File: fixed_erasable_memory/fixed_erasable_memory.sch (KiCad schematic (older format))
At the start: 1 part, among them P1 DIN_41612_128P

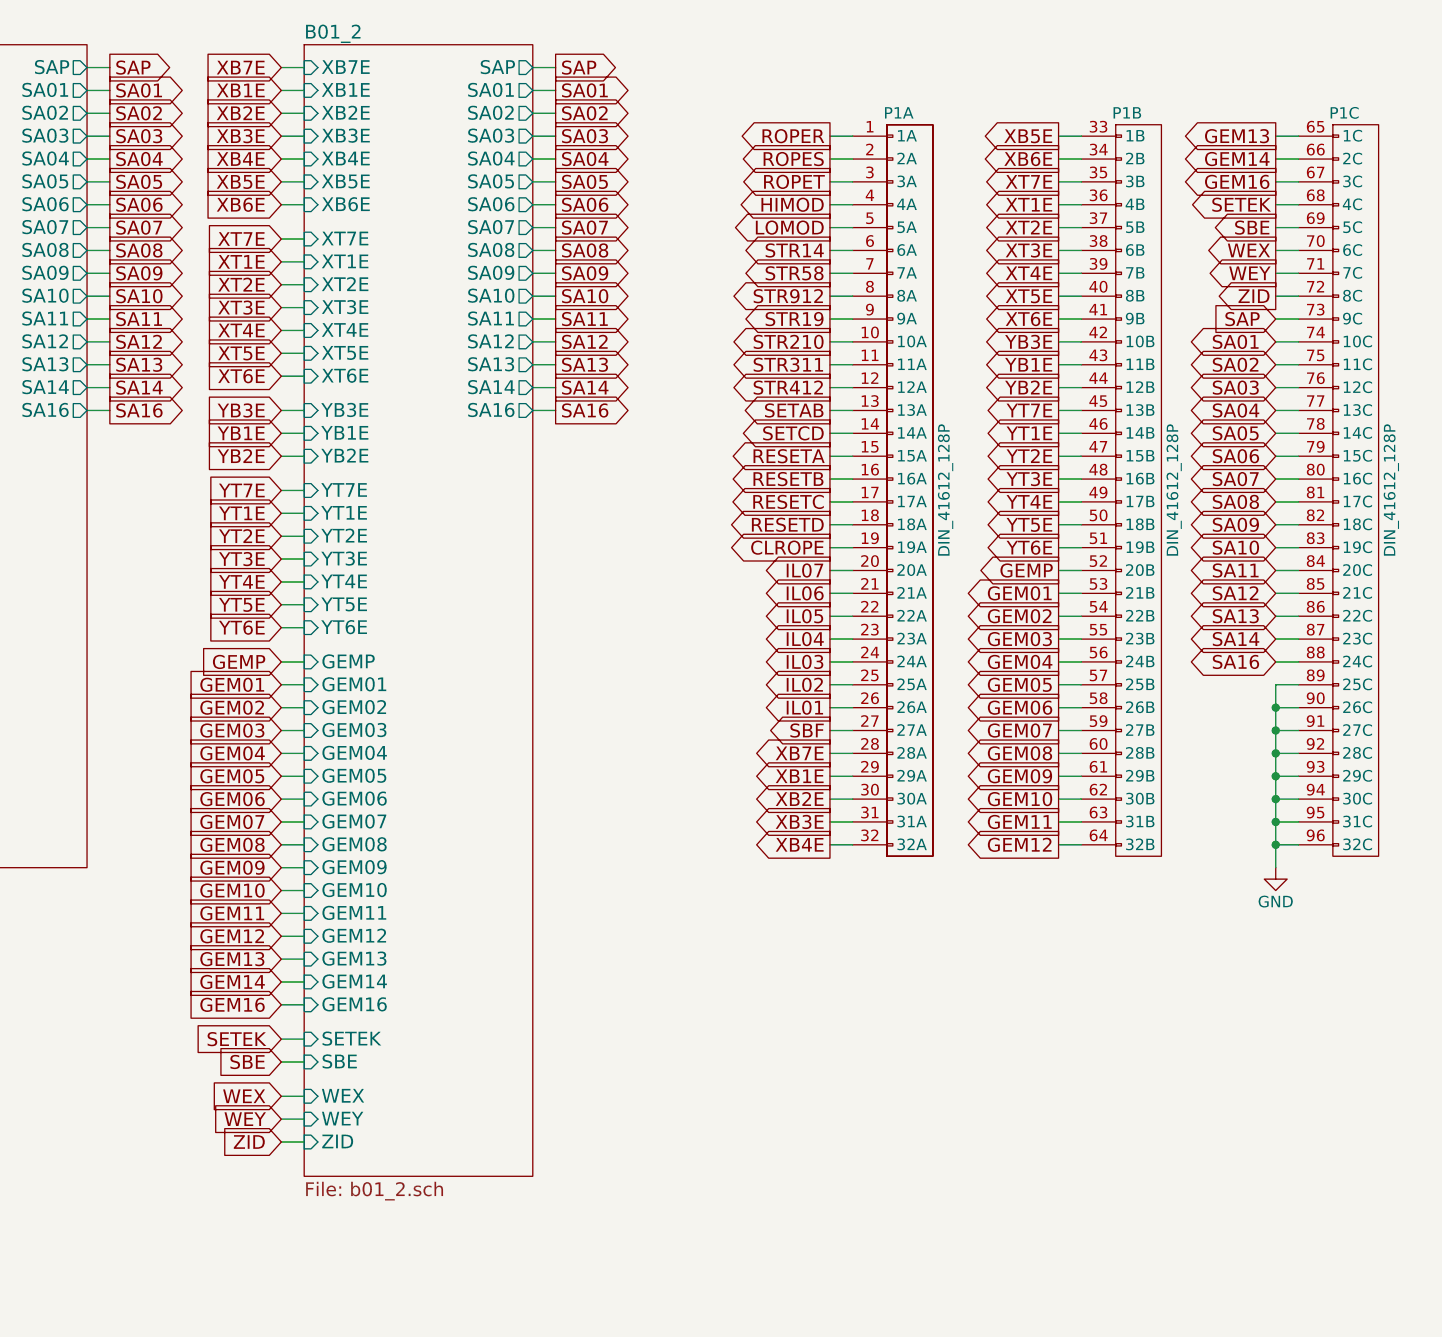
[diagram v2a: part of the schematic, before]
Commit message: Made erasable memory reads destructive, and improved erasable address latching logic
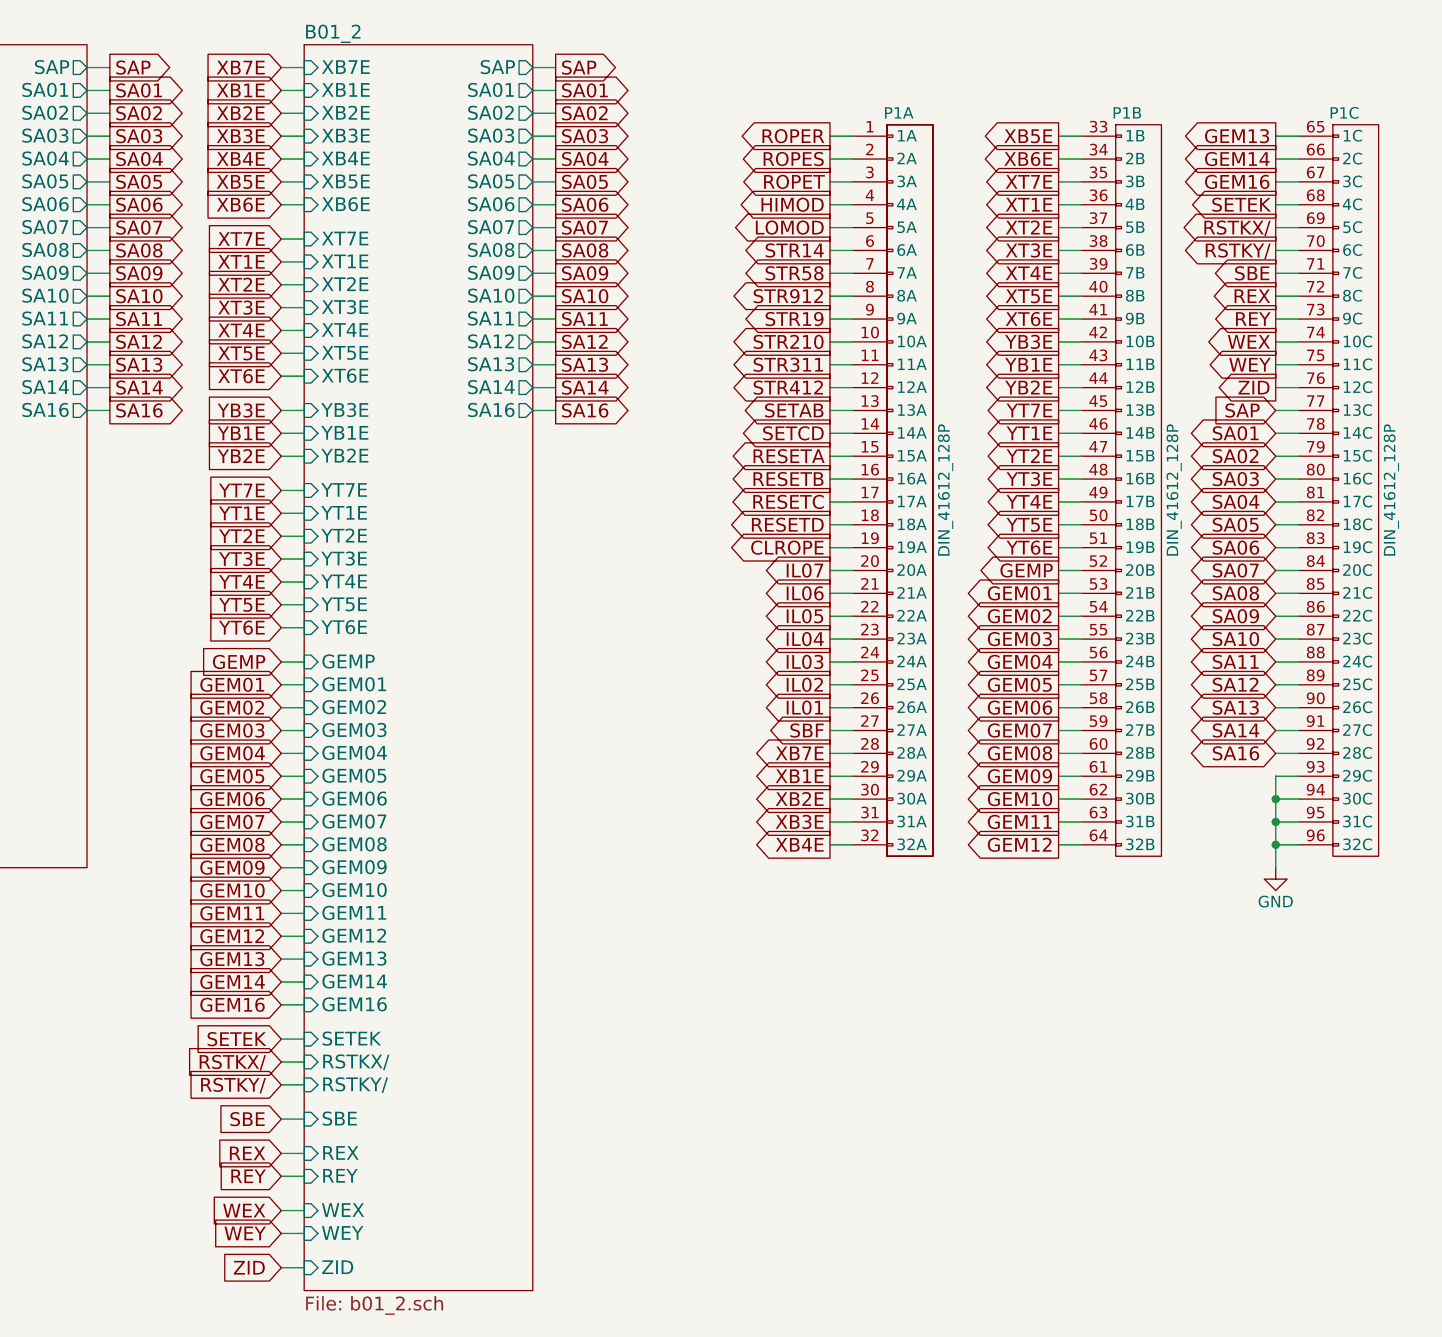
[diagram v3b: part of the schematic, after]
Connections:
- net GND: no longer P1.89 (25C), P1.90 (26C), P1.91 (27C), P1.92 (28C)
- net SA01: now also P1.78 (14C); no longer P1.74 (10C)
- net SA02: now also P1.79 (15C); no longer P1.75 (11C)
- net SA03: now also P1.80 (16C); no longer P1.76 (12C)
- net SA04: now also P1.81 (17C); no longer P1.77 (13C)
- net SA05: now also P1.82 (18C); no longer P1.78 (14C)
- net SA06: now also P1.83 (19C); no longer P1.79 (15C)
- net SA07: now also P1.84 (20C); no longer P1.80 (16C)
- net SA08: now also P1.85 (21C); no longer P1.81 (17C)
- net SA09: now also P1.86 (22C); no longer P1.82 (18C)
- net SA10: now also P1.87 (23C); no longer P1.83 (19C)
- net SA11: now also P1.88 (24C); no longer P1.84 (20C)
- net SA12: now also P1.89 (25C); no longer P1.85 (21C)
- net SA13: now also P1.90 (26C); no longer P1.86 (22C)
- net SA14: now also P1.91 (27C); no longer P1.87 (23C)
- net SA16: now also P1.92 (28C); no longer P1.88 (24C)
- net SAP: now also P1.77 (13C); no longer P1.73 (9C)
- net SBE: now also P1.71 (7C); no longer P1.69 (5C)
- net WEX: now also P1.74 (10C); no longer P1.70 (6C)
- net WEY: now also P1.75 (11C); no longer P1.71 (7C)
- net ZID: now also P1.76 (12C); no longer P1.72 (8C)
- new net REX: P1.72 (8C)
- new net REY: P1.73 (9C)
- new net RSTKX/: P1.69 (5C)
- new net RSTKY/: P1.70 (6C)
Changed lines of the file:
@@
 $EndComp
 Wire Wire Line
-	8450 4400 8550 4400
-Connection ~ 8450 4400
-Wire Wire Line
-	8450 4500 8550 4500
-Connection ~ 8450 4500
-Wire Wire Line
-	8450 4600 8550 4600
-Connection ~ 8450 4600
-Wire Wire Line
 	8450 4700 8550 4700
-Connection ~ 8450 4700
 Wire Wire Line
 	8450 4800 8550 4800
@@
 Wire Wire Line
 	3350 3100 3250 3100
-Text GLabel 8450 2700 0    60   Input ~ 0
+Text GLabel 8450 3100 0    60   Input ~ 0
 SAP
-Wire Wire Line
-	8450 2700 8550 2700
-Text GLabel 8450 2800 0    60   BiDi ~ 0
-SA01
-Wire Wire Line
-	8450 2800 8550 2800
-Text GLabel 8450 2900 0    60   BiDi ~ 0
-SA02
-Wire Wire Line
-	8450 2900 8550 2900
-Text GLabel 8450 3000 0    60   BiDi ~ 0
-SA03
-Wire Wire Line
-	8450 3000 8550 3000
-Text GLabel 8450 3100 0    60   BiDi ~ 0
-SA04
 Wire Wire Line
 	8450 3100 8550 3100
 Text GLabel 8450 3200 0    60   BiDi ~ 0
-SA05
+SA01
 Wire Wire Line
 	8450 3200 8550 3200
 Text GLabel 8450 3300 0    60   BiDi ~ 0
-SA06
+SA02
 Wire Wire Line
 	8450 3300 8550 3300
 Text GLabel 8450 3400 0    60   BiDi ~ 0
-SA07
+SA03
 Wire Wire Line
 	8450 3400 8550 3400
 Text GLabel 8450 3500 0    60   BiDi ~ 0
-SA08
+SA04
 Wire Wire Line
 	8450 3500 8550 3500
 Text GLabel 8450 3600 0    60   BiDi ~ 0
-SA09
+SA05
 Wire Wire Line
 	8450 3600 8550 3600
 Text GLabel 8450 3700 0    60   BiDi ~ 0
-SA10
+SA06
 Wire Wire Line
 	8450 3700 8550 3700
 Text GLabel 8450 3800 0    60   BiDi ~ 0
-SA11
+SA07
 Wire Wire Line
 	8450 3800 8550 3800
 Text GLabel 8450 3900 0    60   BiDi ~ 0
-SA12
+SA08
 Wire Wire Line
 	8450 3900 8550 3900
 Text GLabel 8450 4000 0    60   BiDi ~ 0
-SA13
+SA09
 Wire Wire Line
 	8450 4000 8550 4000
 Text GLabel 8450 4100 0    60   BiDi ~ 0
-SA14
+SA10
 Wire Wire Line
 	8450 4100 8550 4100
 Text GLabel 8450 4200 0    60   BiDi ~ 0
+SA11
+Wire Wire Line
+	8450 4200 8550 4200
+Text GLabel 8450 4300 0    60   BiDi ~ 0
+SA12
+Wire Wire Line
+	8450 4300 8550 4300
+Text GLabel 8450 4400 0    60   BiDi ~ 0
+SA13
+Wire Wire Line
+	8450 4400 8550 4400
+Text GLabel 8450 4500 0    60   BiDi ~ 0
+SA14
+Wire Wire Line
+	8450 4500 8550 4500
+Text GLabel 8450 4600 0    60   BiDi ~ 0
 SA16
 Wire Wire Line
-	8450 4200 8550 4200
+	8450 4600 8550 4600
 Text GLabel 2150 2850 0    60   Input ~ 0
 STR412
@@
 	6500 3700 6600 3700
 $Sheet
-S 4200 1500 1000 4950
+S 4200 1500 1000 5450
 U 56D35FA5
 F0 "B01_2" 60
@@
 F24 "YT5E" I L 4200 3950 60
 F25 "YT3E" I L 4200 3750 60
-F26 "ZID" I L 4200 6300 60
+F26 "ZID" I L 4200 6850 60
 F27 "GEMP" I L 4200 4200 60
 F28 "GEM01" I L 4200 4300 60
@@
 F57 "SA14" O R 5200 3000 60
 F58 "SA16" O R 5200 3100 60
-F59 "WEX" I L 4200 6100 60
-F60 "WEY" I L 4200 6200 60
-F61 "SBE" I L 4200 5950 60
+F59 "WEX" I L 4200 6600 60
+F60 "WEY" I L 4200 6700 60
+F61 "SBE" I L 4200 6200 60
 F62 "SETEK" I L 4200 5850 60
+F63 "RSTKX/" I L 4200 5950 60
+F64 "RSTKY/" I L 4200 6050 60
+F65 "REX" I L 4200 6350 60
+F66 "REY" I L 4200 6450 60
 $EndSheet
 Text GLabel 5300 1600 2    60   Output ~ 0
@@
 Wire Wire Line
 	8450 2100 8550 2100
+Text GLabel 4100 6200 0    60   Input ~ 0
+SBE
+Wire Wire Line
+	4100 6200 4200 6200
+Text GLabel 4100 6600 0    60   Input ~ 0
+WEX
+Wire Wire Line
+	4100 6600 4200 6600
+Text GLabel 4100 6700 0    60   Input ~ 0
+WEY
+Wire Wire Line
+	4100 6700 4200 6700
+Text GLabel 4100 6850 0    60   Input ~ 0
+ZID
+Wire Wire Line
+	4100 6850 4200 6850
+Text GLabel 8450 2500 0    60   Output ~ 0
+SBE
+Wire Wire Line
+	8450 2500 8550 2500
+Text GLabel 8450 2800 0    60   Output ~ 0
+WEX
+Wire Wire Line
+	8450 2800 8550 2800
+Text GLabel 8450 2900 0    60   Output ~ 0
+WEY
+Wire Wire Line
+	8450 2900 8550 2900
+Text GLabel 8450 3000 0    60   Output ~ 0
+ZID
+Wire Wire Line
+	8450 3000 8550 3000
+Text GLabel 4100 5850 0    60   Input ~ 0
+SETEK
+Wire Wire Line
+	4100 5850 4200 5850
+Text GLabel 8450 2200 0    60   Output ~ 0
+SETEK
+Wire Wire Line
+	8450 2200 8550 2200
 Text GLabel 4100 5950 0    60   Input ~ 0
-SBE
+RSTKX/
 Wire Wire Line
 	4100 5950 4200 5950
-Text GLabel 4100 6100 0    60   Input ~ 0
-WEX
-Wire Wire Line
-	4100 6100 4200 6100
-Text GLabel 4100 6200 0    60   Input ~ 0
-WEY
-Wire Wire Line
-	4100 6200 4200 6200
-Text GLabel 4100 6300 0    60   Input ~ 0
-ZID
-Wire Wire Line
-	4100 6300 4200 6300
+Text GLabel 4100 6050 0    60   Input ~ 0
+RSTKY/
+Wire Wire Line
+	4100 6050 4200 6050
+Text GLabel 4100 6350 0    60   Input ~ 0
+REX
+Wire Wire Line
+	4100 6350 4200 6350
+Text GLabel 4100 6450 0    60   Input ~ 0
+REY
+Wire Wire Line
+	4100 6450 4200 6450
 Text GLabel 8450 2300 0    60   Output ~ 0
-SBE
+RSTKX/
 Wire Wire Line
 	8450 2300 8550 2300
 Text GLabel 8450 2400 0    60   Output ~ 0
-WEX
+RSTKY/
 Wire Wire Line
 	8450 2400 8550 2400
-Text GLabel 8450 2500 0    60   Output ~ 0
-WEY
-Wire Wire Line
-	8450 2500 8550 2500
 Text GLabel 8450 2600 0    60   Output ~ 0
-ZID
+REX
 Wire Wire Line
 	8450 2600 8550 2600
-Wire Wire Line
-	8450 4300 8550 4300
-Text GLabel 4100 5850 0    60   Input ~ 0
-SETEK
-Wire Wire Line
-	4100 5850 4200 5850
-Wire Wire Line
-	8450 4300 8450 5100
-Text GLabel 8450 2200 0    60   Output ~ 0
-SETEK
-Wire Wire Line
-	8450 2200 8550 2200
+Text GLabel 8450 2700 0    60   Output ~ 0
+REY
+Wire Wire Line
+	8450 2700 8550 2700
+Wire Wire Line
+	8450 4700 8450 5100
 $EndSCHEMATC

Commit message: Fixed/erasable memory on switched power, and voltage pin updates for the memories and tristate buffers
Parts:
- added U31002, U31011, U31012, U31015, U31016, U31027, U31037, U31038, U31041: 74HC04, symbol 74HC04
- added U31003, U31004, U31007, U31008: 74HC27, symbol 74HC27
- added U31005, U31009, U31010, U31014, U31017, U31018, U31026, U31028, U31029, U31030, U31031, U31032, U31033, U31034, U31035, U31036, U31039, U31040: 74HC02, symbol 74HC02
- added U31006, U31013, U31019, U31020, U31021, U31022: 74HC4002, symbol 74HC4002
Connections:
- net labels added: +4VSW
- net labels removed: VCC
- wire segments 305 -> 313
